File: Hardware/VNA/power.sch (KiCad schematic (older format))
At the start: 41 parts, among them Q1 RE1C002UN, U4 LP5912, U5 LP5912, U6 MIC5366-1.8

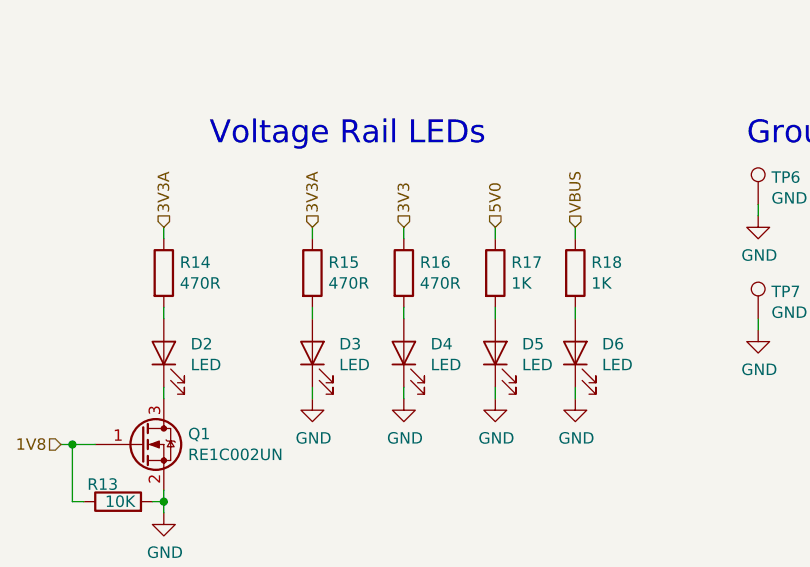
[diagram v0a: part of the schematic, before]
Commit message: FW for V0 init, functinal diagram / schematic updated freq ranges
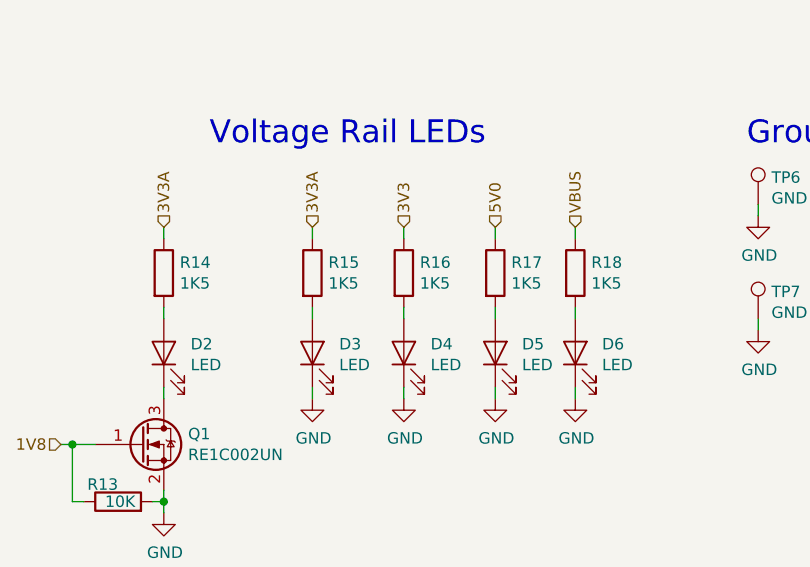
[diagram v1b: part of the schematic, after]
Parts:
- R14, R15, R16: value 470R -> 1K5
- R17, R18: value 1K -> 1K5
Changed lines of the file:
@@
 P 6600 2750
 F 0 "R14" H 6670 2796 50  0000 L CNN
-F 1 "470R" H 6670 2705 50  0000 L CNN
+F 1 "1K5" H 6670 2705 50  0000 L CNN
 F 2 "Resistor_SMD:R_0603_1608Metric" V 6530 2750 50  0001 C CNN
 F 3 "~" H 6600 2750 50  0001 C CNN
@@
 P 7250 2750
 F 0 "R15" H 7320 2796 50  0000 L CNN
-F 1 "470R" H 7320 2705 50  0000 L CNN
+F 1 "1K5" H 7320 2705 50  0000 L CNN
 F 2 "Resistor_SMD:R_0603_1608Metric" V 7180 2750 50  0001 C CNN
 F 3 "~" H 7250 2750 50  0001 C CNN
@@
 P 7650 2750
 F 0 "R16" H 7720 2796 50  0000 L CNN
-F 1 "470R" H 7720 2705 50  0000 L CNN
+F 1 "1K5" H 7720 2705 50  0000 L CNN
 F 2 "Resistor_SMD:R_0603_1608Metric" V 7580 2750 50  0001 C CNN
 F 3 "~" H 7650 2750 50  0001 C CNN
@@
 P 8050 2750
 F 0 "R17" H 8120 2796 50  0000 L CNN
-F 1 "1K" H 8120 2705 50  0000 L CNN
+F 1 "1K5" H 8120 2705 50  0000 L CNN
 F 2 "Resistor_SMD:R_0603_1608Metric" V 7980 2750 50  0001 C CNN
 F 3 "~" H 8050 2750 50  0001 C CNN
@@
 P 8400 2750
 F 0 "R18" H 8470 2796 50  0000 L CNN
-F 1 "1K" H 8470 2705 50  0000 L CNN
+F 1 "1K5" H 8470 2705 50  0000 L CNN
 F 2 "Resistor_SMD:R_0603_1608Metric" V 8330 2750 50  0001 C CNN
 F 3 "~" H 8400 2750 50  0001 C CNN
